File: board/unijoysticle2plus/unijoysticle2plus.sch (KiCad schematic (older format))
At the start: 42 parts, among them J1 DB9_Female, J2 DB9_Female, J3 USB_B_Micro, Q1 S8050, Q2 S8050, SW1 RESET, SW2 JOY SWAP, SW3 BOOT, U1 74HC05, U2 74HC05, U3 74HC05, U4 ESP32-WROOM-32E, U5 AMS1117-3.3, U6 CH340B/C

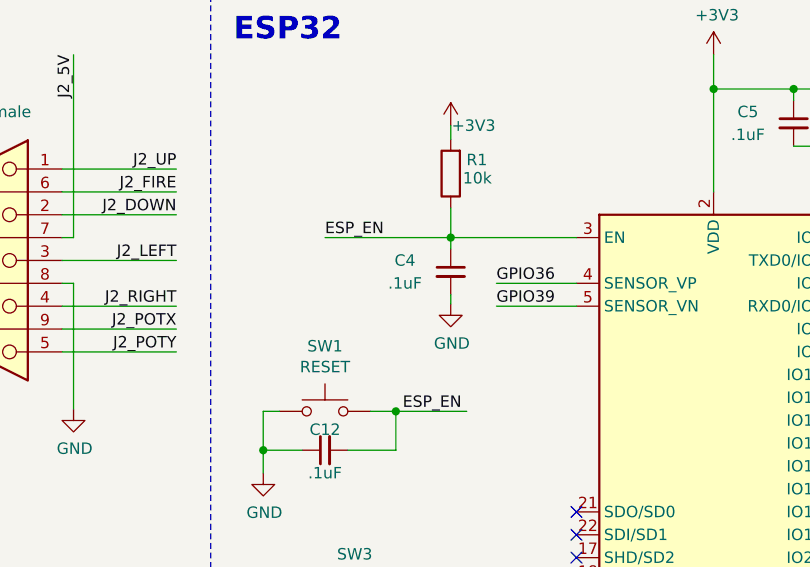
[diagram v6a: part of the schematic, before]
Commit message: Unijoysticle 2+: use 10uF cap for C4
Instead of using .1uF cap for C4, it is replaced with a 10uF.
This fixes the autoboot issues.
Yay!
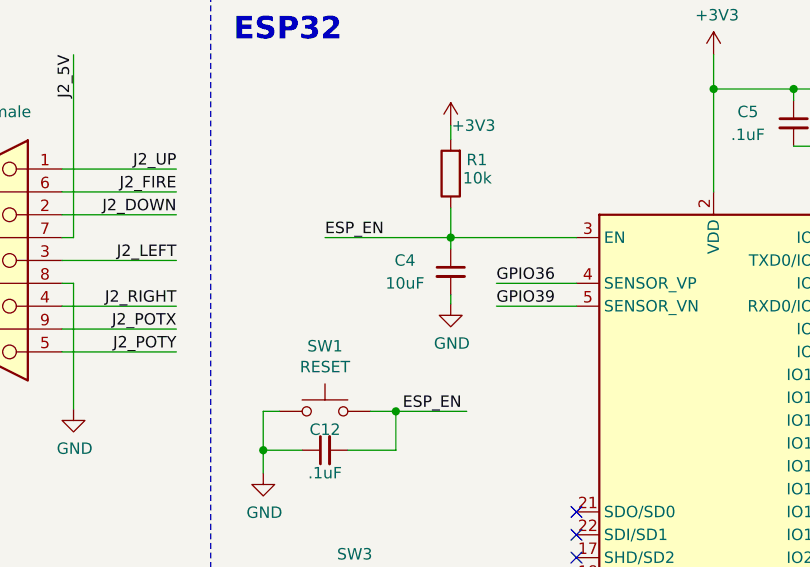
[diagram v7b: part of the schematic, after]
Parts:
- C4: value .1uF -> 10uF; LCSC C49678 -> C15850
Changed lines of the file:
@@
 Sheet 1 1
 Title "Unijoysticle 2+"
-Date "2021-08-07"
-Rev "E"
+Date "2021-10-03"
+Rev "F"
 Comp "Retro Moe"
 Comment1 ""
@@
 P 4100 1700
 F 0 "C4" H 3900 1750 50  0000 C CNN
-F 1 ".1uF" H 3900 1650 50  0000 C CNN
+F 1 "10uF" H 3900 1650 50  0000 C CNN
 F 2 "Capacitor_SMD:C_0805_2012Metric_Pad1.18x1.45mm_HandSolder" H 4100 1700 50  0001 C CNN
 F 3 "~" H 4100 1700 50  0001 C CNN
-F 4 "C49678" H 4100 1700 50  0001 C CNN "LCSC"
+F 4 "C15850" H 4100 1700 50  0001 C CNN "LCSC"
 	1    4100 1700
 	1    0    0    -1

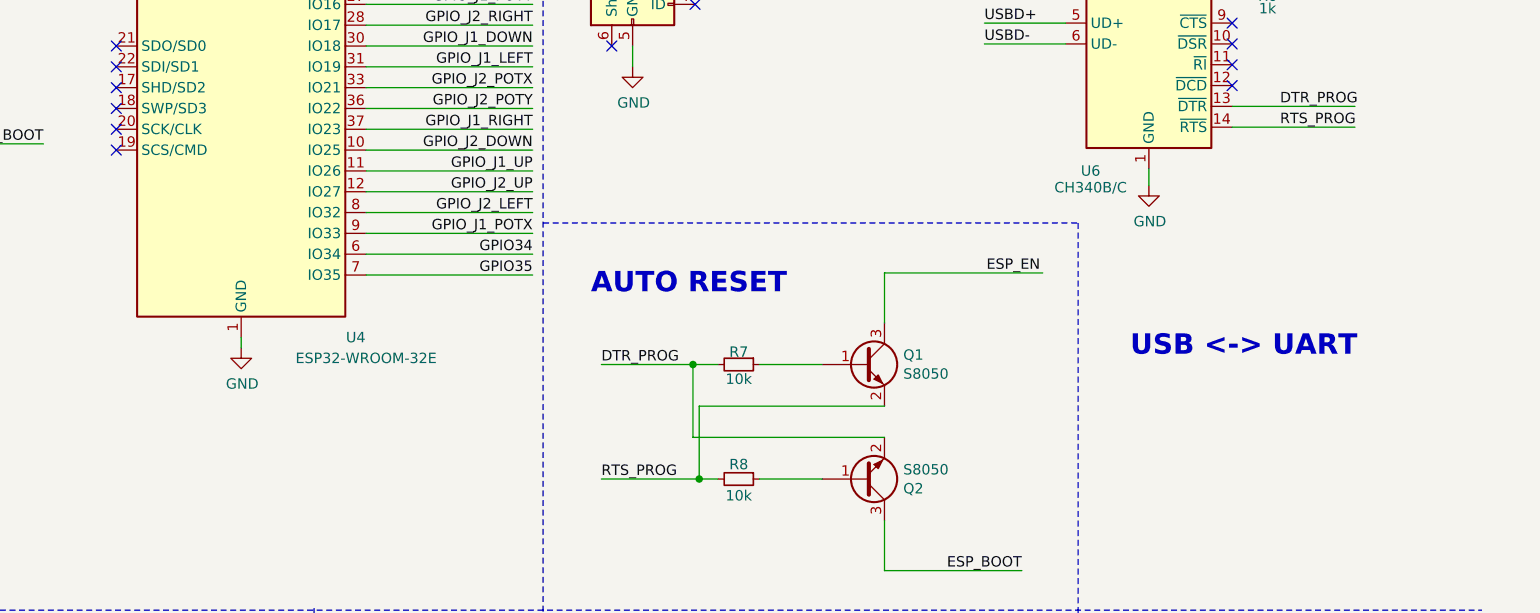
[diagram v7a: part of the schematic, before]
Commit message: Unijoysticle2+: add text in schematic about ch340 and ESP32
Either CH340B or CH340C can be used.
And any ESP32-WROOM-32 can be used: 32, 32D or 32E (not the "U" variant
of course)
Add "JLCJLCJLCJLC" in silk screen to place the order number there.
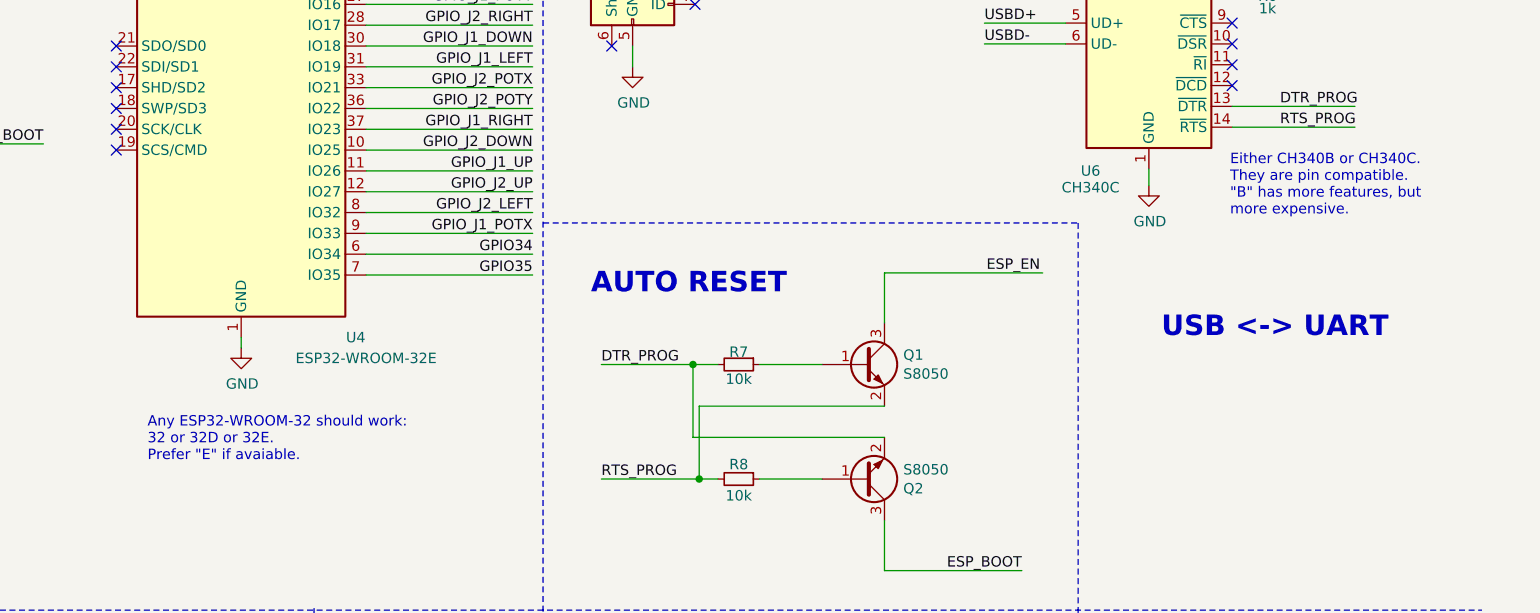
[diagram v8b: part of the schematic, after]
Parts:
- U4: LCSC C473012 -> C82899
- U6: value CH340B/C -> CH340C; LCSC C81010 -> C84681
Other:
- note added: "Any ESP32-WROOM-32 should work:\n32 or 32D or 32E.\nPrefer "E" if avaiable."
- note added: "Either CH340B or CH340C.\nThey are pin compatible.\n"B" has more features, but\nmore expensive."
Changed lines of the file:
@@
 F 2 "RF_Module:ESP32-WROOM-32" H 5250 1250 50  0001 C CNN
 F 3 "https://www.espressif.com/sites/default/files/documentation/esp32-wroom-32d_esp32-wroom-32u_datasheet_en.pdf" H 4950 2800 50  0001 C CNN
-F 4 "C473012" H 5250 2750 50  0001 C CNN "LCSC"
+F 4 "C82899" H 5250 2750 50  0001 C CNN "LCSC"
 	1    5250 2750
 	1    0    0    -1
@@
 Text Notes 6850 1650 0    98   ~ 20
 POWER
-Text Notes 9520 4250 0    98   ~ 20
+Text Notes 9670 4160 0    98   ~ 20
 USB <-> UART
 Text Notes 3150 700  0    98   ~ 20
@@
 P 9610 2740
 F 0 "U6" H 9330 2130 50  0000 C CNN
-F 1 "CH340B/C" H 9330 2050 50  0000 C CNN
+F 1 "CH340C" H 9330 2050 50  0000 C CNN
 F 2 "Package_SO:SOIC-16_3.9x9.9mm_P1.27mm" H 9660 2190 50  0001 L CNN
 F 3 "https://datasheet.lcsc.com/szlcsc/Jiangsu-Qin-Heng-CH340C_C84681.pdf" H 9260 3540 50  0001 C CNN
-F 4 "C81010" H 9610 2740 50  0001 C CNN "LCSC"
+F 4 "C84681" H 9610 2740 50  0001 C CNN "LCSC"
 	1    9610 2740
 	1    0    0    -1
@@
 	1    0    0    -1
 $EndComp
+Text Notes 10000 3570 0    50   ~ 0
+Either CH340B or CH340C.\nThey are pin compatible.\n"B" has more features, but\nmore expensive.
+Text Notes 4800 4750 0    50   ~ 0
+Any ESP32-WROOM-32 should work:\n32 or 32D or 32E.\nPrefer "E" if avaiable.
 $EndSCHEMATC
